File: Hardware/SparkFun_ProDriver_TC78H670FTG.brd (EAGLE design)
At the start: 50.8 x 57.1 mm, 93 parts, among them J2 LATCH, J3 PTH, J4 LATCH, J5 LATCH, J6 PTH, J7 LATCH, J8 PTH, U1 TC78H670FTG, U2 LM1117

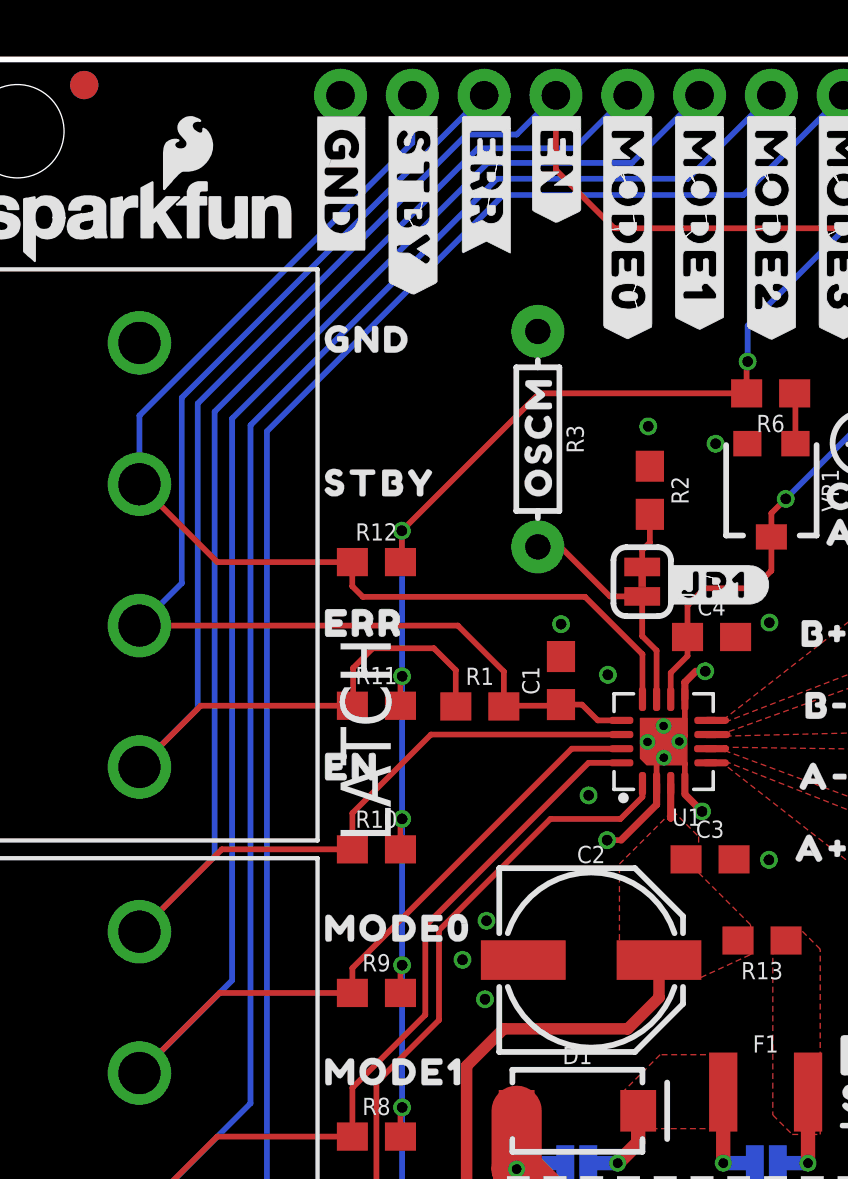
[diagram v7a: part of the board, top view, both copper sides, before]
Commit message: bplace labels done
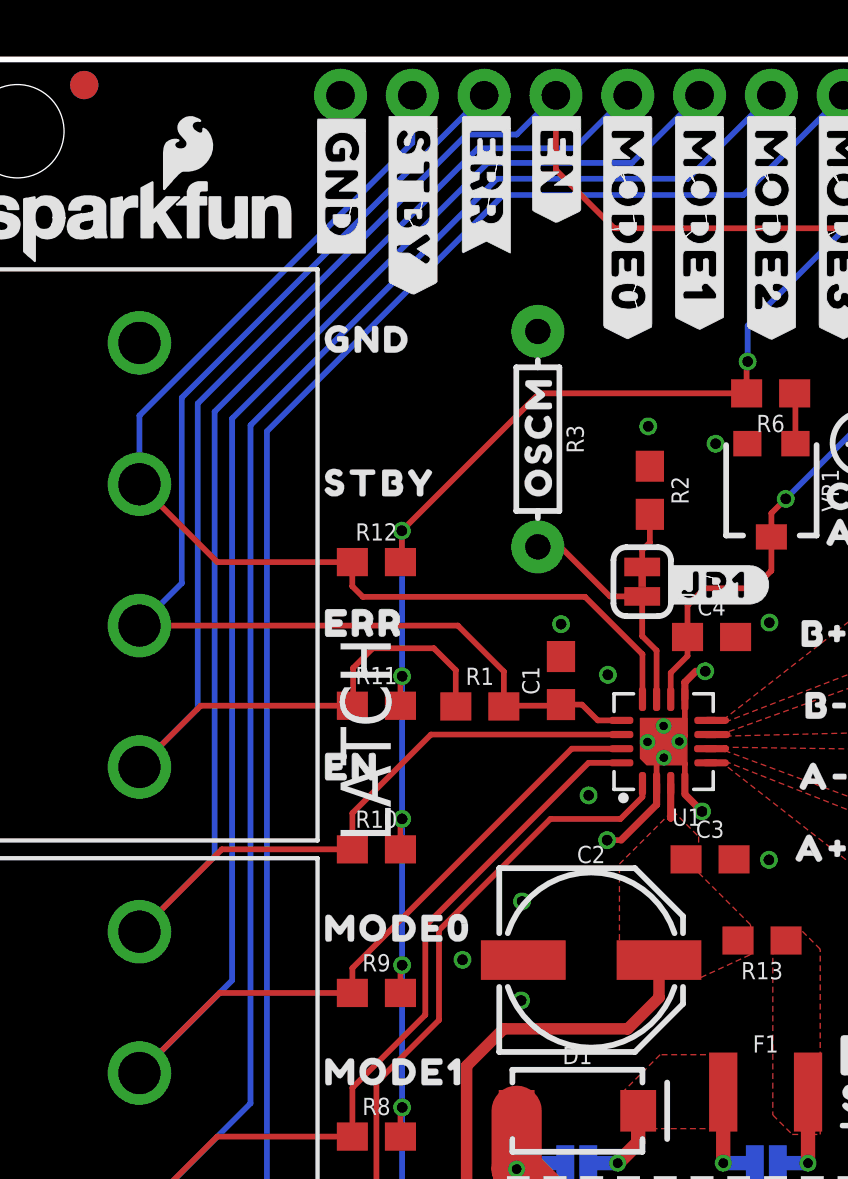
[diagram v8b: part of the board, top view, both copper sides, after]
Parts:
- removed U$39: (no value), output:#PTC_BP#0
- added U$37, U$56: (no value), output:#B##0
- added U$49, U$57: (no value), output:#B##1
- added U$50, U$58: (no value), output:#A##2
- added U$51, U$59: (no value), output:#A##3
- added U$52, U$70: (no value), output:#GND#5
- added U$53: (no value), output:#STBY#0
- added U$54: (no value), output:#ERR#0
- added U$55: (no value), output:#_EN_#0
- added U$60: (no value), output:#MODE0#0
- added U$61: (no value), output:#MODE1#0
- added U$62: (no value), output:#MODE2#0
- added U$63: (no value), output:#MODE3#0
- added U$64: (no value), output:#PTC_BP#0
- added U$65: (no value), output:#CLK#S_CLK#0
- added U$66: (no value), output:#SET_EN#LATCH#0
- added U$67: (no value), output:#UP#DW#S_DATA#0
- added U$68, U$72: (no value), output:#VM#0
- added U$69, U$73: (no value), output:#GND#0
- added U$71: (no value), output:#ERR#3
- added U$74: (no value), output:#STBY#1
- added U$75: (no value), output:#EN#4
- added U$76: (no value), output:#MODE0#4
- added U$77: (no value), output:#MODE1#4
- added U$78: (no value), output:#MODE2#4
- added U$79: (no value), output:#MODE3#4
- added U$80: (no value), output:#3V3#4
- added U$81: (no value), output:#VREF#0
- added U$82: (no value), output:#CW#CCW#0
- moved U$31 2.88 mm to (14.0, 52.7)
- moved U$38 1.00 mm to (22.3, 17.4), turned to 270 degrees
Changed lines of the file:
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@@
 <setting verticaltext="up"/>
 </settings>
-<grid distance="0.05" unitdist="inch" unit="inch" style="lines" multiple="1" display="yes" altdistance="0.001" altunitdist="inch" altunit="inch"/>
+<grid distance="0.05" unitdist="inch" unit="inch" style="lines" multiple="1" display="yes" altdistance="0.0001" altunitdist="inch" altunit="inch"/>
 <layers>
 <layer number="1" name="Top" color="4" fill="1" visible="yes" active="yes"/>
@@
 <wire x1="44.0182" y1="43.1546" x2="32.766" y2="38.9128" width="0.2032" layer="41"/>
 <wire x1="32.766" y1="38.9128" x2="26.6446" y2="34.163" width="0.2032" layer="41"/>
+<rectangle x1="49.32171875" y1="39.677340625" x2="50.69331875" y2="41.401996875" layer="22"/>
+<rectangle x1="43.837859375" y1="34.67608125" x2="46.649640625" y2="36.40328125" layer="22"/>
+<rectangle x1="49.222659375" y1="34.678621875" x2="50.695859375" y2="36.403278125" layer="22"/>
+<rectangle x1="43.804840625" y1="39.677340625" x2="46.606459375" y2="41.401996875" layer="22"/>
+<rectangle x1="43.61941875" y1="29.6799" x2="46.3677" y2="31.40455625" layer="22"/>
+<rectangle x1="49.25821875" y1="29.6799" x2="50.69078125" y2="31.40201875" layer="22"/>
+<rectangle x1="43.822621875" y1="24.678640625" x2="46.233078125" y2="26.400759375" layer="22"/>
+<rectangle x1="49.189640625" y1="24.678640625" x2="50.683159375" y2="26.400759375" layer="22"/>
+<rectangle x1="4.874259375" y1="36.179759375" x2="6.70051875" y2="37.9095" layer="22"/>
+<rectangle x1="0.099059375" y1="36.1823" x2="0.835659375" y2="37.9095" layer="22"/>
+<rectangle x1="4.803140625" y1="31.242" x2="6.644640625" y2="32.971740625" layer="22"/>
+<rectangle x1="0.1016" y1="31.242" x2="0.97028125" y2="32.971740625" layer="22"/>
+<rectangle x1="40.993059375" y1="5.02158125" x2="42.720259375" y2="6.30681875" layer="22"/>
+<rectangle x1="40.993059375" y1="0.099059375" x2="42.7228" y2="0.73151875" layer="22"/>
+<rectangle x1="36.01974375" y1="0.116840625" x2="37.73678125" y2="1.163321875" layer="22"/>
+<rectangle x1="36.0146625" y1="4.66598125" x2="37.7418625" y2="6.16711875" layer="22"/>
+<rectangle x1="5.12571875" y1="46.230540625" x2="6.644640625" y2="47.957740625" layer="22"/>
+<rectangle x1="0.1016" y1="46.23308125" x2="0.7747" y2="47.9552" layer="22"/>
 </plain>
 <attributes>
@@
 <element name="U$6" library="output" package="TC78H670FTG0" value="" x="30.934653125" y="19.052534375" smashed="yes"/>
 <element name="U$9" library="output" package="STEPPER_MOTOR_DRIVER0" value="" x="31.000690625" y="20.393653125" smashed="yes"/>
-<element name="U$31" library="output" package="#GND#0" value="" x="13.9954" y="55.5498" smashed="yes" rot="R270"/>
+<element name="U$31" library="output" package="#GND#0" value="" x="14.0081" y="52.6694375" smashed="yes" rot="R270"/>
 <element name="U$40" library="output" package="PRODRIVER0" value="" x="30.55619375" y="21.91765625" smashed="yes"/>
 <element name="U$41" library="output" package="#_POWER_INPUT_2#5#16V_#0" value="" x="32.766" y="17.571721875" smashed="yes"/>
@@
 <attribute name="VALUE" x="22.3266" y="19.2532" size="0.6096" layer="28" font="vector" ratio="20" rot="MR180" align="top-center"/>
 </element>
-<element name="U$38" library="output" package="#D1_BP#0" value="" x="21.5138" y="18.0594" smashed="yes" rot="MR0"/>
-<element name="U$39" library="output" package="#PTC_BP#0" value="" x="36.5252" y="18.1102" smashed="yes" rot="MR0"/>
+<element name="U$38" library="output" package="#D1_BP#0" value="" x="22.30628125" y="17.44471875" smashed="yes" rot="MR270"/>
+<element name="U$37" library="output" package="#B##0" value="" x="49.8475" y="40.540940625" smashed="yes" rot="MR0"/>
+<element name="U$49" library="output" package="#B##1" value="" x="49.8475" y="35.53968125" smashed="yes" rot="MR0"/>
+<element name="U$50" library="output" package="#A##2" value="" x="49.7713" y="30.5435" smashed="yes" rot="MR0"/>
+<element name="U$51" library="output" package="#A##3" value="" x="49.811940625" y="25.5397" smashed="yes" rot="MR0"/>
+<element name="U$52" library="output" package="#GND#5" value="" x="2.95401875" y="47.09668125" smashed="yes" rot="MR0"/>
+<element name="U$53" library="output" package="#STBY#0" value="" x="2.910840625" y="42.07001875" smashed="yes" rot="MR0"/>
+<element name="U$54" library="output" package="#ERR#0" value="" x="2.87528125" y="37.048440625" smashed="yes" rot="MR0"/>
+<element name="U$55" library="output" package="#_EN_#0" value="" x="2.900678125" y="32.108140625" smashed="yes" rot="MR0"/>
+<element name="U$56" library="output" package="#B##0" value="" x="32.705040625" y="36.78681875" smashed="yes" rot="MR0"/>
+<element name="U$57" library="output" package="#B##1" value="" x="32.705040625" y="34.24681875" smashed="yes" rot="MR0"/>
+<element name="U$58" library="output" package="#A##2" value="" x="32.705040625" y="31.70681875" smashed="yes" rot="MR0"/>
+<element name="U$59" library="output" package="#A##3" value="" x="32.705040625" y="29.16681875" smashed="yes" rot="MR0"/>
+<element name="U$60" library="output" package="#MODE0#0" value="" x="2.898140625" y="26.17978125" smashed="yes" rot="MR0"/>
+<element name="U$61" library="output" package="#MODE1#0" value="" x="3.020059375" y="21.206459375" smashed="yes" rot="MR0"/>
+<element name="U$62" library="output" package="#MODE2#0" value="" x="2.89051875" y="16.20011875" smashed="yes" rot="MR0"/>
+<element name="U$63" library="output" package="#MODE3#0" value="" x="2.834640625" y="11.211559375" smashed="yes" rot="MR0"/>
+<element name="U$65" library="output" package="#CLK#S_CLK#0" value="" x="12.573" y="16.3068" smashed="yes" rot="MR0"/>
+<element name="U$66" library="output" package="#SET_EN#LATCH#0" value="" x="14.3256" y="21.282659375" smashed="yes" rot="MR0"/>
+<element name="U$67" library="output" package="#UP#DW#S_DATA#0" value="" x="14.488159375" y="26.253440625" smashed="yes" rot="MR0"/>
+<element name="U$68" library="output" package="#VM#0" value="" x="46.78171875" y="11.34618125" smashed="yes" rot="MR0"/>
+<element name="U$69" library="output" package="#GND#0" value="" x="46.370240625" y="8.82141875" smashed="yes" rot="MR0"/>
+<element name="U$70" library="output" package="#GND#5" value="" x="14.0081" y="52.664359375" smashed="yes" rot="MR270"/>
+<element name="U$72" library="output" package="#VM#0" value="" x="36.878265625" y="2.93624375" smashed="yes" rot="MR90"/>
+<element name="U$73" library="output" package="#GND#0" value="" x="41.856659375" y="2.94131875" smashed="yes" rot="MR90"/>
+<element name="U$74" library="output" package="#STBY#1" value="" x="16.537940625" y="55.5371" smashed="yes" rot="MR270"/>
+<element name="U$71" library="output" package="#ERR#3" value="" x="19.077940625" y="55.5371" smashed="yes" rot="MR270"/>
+<element name="U$75" library="output" package="#EN#4" value="" x="21.617940625" y="55.5371" smashed="yes" rot="MR270"/>
+<element name="U$76" library="output" package="#MODE0#4" value="" x="24.13" y="55.5498" smashed="yes" rot="MR270"/>
+<element name="U$77" library="output" package="#MODE1#4" value="" x="26.67" y="55.5498" smashed="yes" rot="MR270"/>
+<element name="U$78" library="output" package="#MODE2#4" value="" x="29.21" y="55.5498" smashed="yes" rot="MR270"/>
+<element name="U$79" library="output" package="#MODE3#4" value="" x="31.75" y="55.5498" smashed="yes" rot="MR270"/>
+<element name="U$80" library="output" package="#3V3#4" value="" x="34.29" y="55.5498" smashed="yes" rot="MR270"/>
+<element name="U$81" library="output" package="#VREF#0" value="" x="36.83" y="55.4736" smashed="yes" rot="MR270"/>
+<element name="U$82" library="output" package="#CW#CCW#0" value="" x="11.52651875" y="11.2649" smashed="yes" rot="MR0"/>
+<element name="U$64" library="output" package="#PTC_BP#0" value="" x="29.02711875" y="17.48281875" smashed="yes" rot="MR270"/>
 </elements>
 <signals>
@@
 <via x="26.87065625" y="35.5092" extent="1-16" drill="0.381"/>
 <via x="21.770334375" y="37.175440625" extent="1-16" drill="0.381"/>
-<via x="19.133815625" y="26.682703125" extent="1-16" drill="0.381"/>
-<via x="19.080475" y="23.906484375" extent="1-16" drill="0.381"/>
+<via x="20.391115625" y="27.368503125" extent="1-16" drill="0.381"/>
+<via x="20.35809375" y="23.86584375" extent="1-16" drill="0.381"/>
 <via x="29.123634375" y="28.839165625" extent="1-16" drill="0.381"/>
 <via x="30.459675" y="11.170925" extent="1-16" drill="0.381"/>
@@
 <contactref element="J4" pad="3"/>
 <contactref element="J6" pad="9"/>
-<wire x1="16.51" y1="54.2036" x2="16.51" y2="55.88" width="0.2032" layer="16"/>
 <wire x1="6.858" y1="44.5516" x2="16.51" y2="54.2036" width="0.2032" layer="16"/>
 <wire x1="6.858" y1="42.124" x2="6.858" y2="44.5516" width="0.2032" layer="16"/>
 <wire x1="6.858" y1="42.124" x2="9.612" y2="39.37" width="0.2032" layer="1"/>
+<wire x1="16.51" y1="54.2036" x2="16.51" y2="55.88" width="0.2032" layer="16"/>
 </signal>
 <signal name="MODE3">
